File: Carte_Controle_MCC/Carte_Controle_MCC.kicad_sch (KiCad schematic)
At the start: 31 parts, among them J1 USB_C_Receptacle_USB2.0_16P, J2 Conn_ST_STDC14, J3 Conn_01x02_XT60, J4 Conn_01x04_moteur, U1 USBLC6-2SC6, U2 STM32G431CBUx

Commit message: Update 2
Correction of the schematic,
creation of new footprints,
Association of the footprints and the symbols
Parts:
- added H1, H2, H3, H4: MountingHole_Pad, MountingHole:MountingHole_3.2mm_M3_DIN965_Pad, symbol Mechanical:MountingHole_Pad
- C1, C10, C11, C2, C3, C4, C5, C6, C7, C8, C9: footprint (none) -> Capacitor_SMD:C_0201_0603Metric_Pad0.64x0.40mm_HandSolder
- C_IN1: renamed from C_IN; footprint (none) -> Capacitor_SMD:C_0201_0603Metric_Pad0.64x0.40mm_HandSolder
- C_OUT1: renamed from C_OUT; footprint (none) -> Capacitor_SMD:C_0201_0603Metric_Pad0.64x0.40mm_HandSolder
- C_VCC1: renamed from C_VCC; footprint (none) -> Capacitor_SMD:C_0201_0603Metric_Pad0.64x0.40mm_HandSolder
- D1, D2: footprint (none) -> Diode_SMD:D_0603_1608Metric_Pad1.05x0.95mm_HandSolder
- J1: footprint (none) -> Connector_USB:USB_C_Receptacle_G-Switch_GT-USB-7010ASV
- J2: footprint (none) -> Connector_PinHeader_1.27mm:PinHeader_2x07_P1.27mm_Vertical_SMD
- J3: footprint (none) -> Connector_AMASS:AMASS_XT60-M_1x02_P7.20mm_Vertical
- J4: footprint (none) -> Connector_JST:JST_EH_B4B-EH-A_1x04_P2.50mm_Vertical
- L1: footprint (none) -> Inductor_SMD:L_0805_2012Metric_Pad1.05x1.20mm_HandSolder
- R1, R2: value R_Small -> 5.1k; footprint (none) -> Resistor_SMD:R_0603_1608Metric_Pad0.98x0.95mm_HandSolder
- R_FBB1: renamed from R_FBB; footprint (none) -> Resistor_SMD:R_0603_1608Metric_Pad0.98x0.95mm_HandSolder
- R_FBT1: renamed from R_FBT; footprint (none) -> Resistor_SMD:R_0603_1608Metric_Pad0.98x0.95mm_HandSolder
- R_SW1: renamed from R_SW; footprint (none) -> Resistor_SMD:R_0603_1608Metric_Pad0.98x0.95mm_HandSolder
- U3: footprint (none) -> maker:wurth_171013801
- U4: footprint (none) -> maker:Gate_Driver_MIC4606-2YTS-TR
- U5: footprint (none) -> maker:Mosfet_FDMQ86530L
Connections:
- net USART_TX is gone; now on net USART_Tx: U2.31 (PA9)
- net +15V: now also U5.13 (D1/D4)
- net GND: now also U2.49 (VSS), H1.1, H2.1, H3.1, H4.1
- net S1/D2_INPUT: now also U5.14 (S1/D2)
- net S4/D3_INPUT: now also U5.15 (D3/S4)
- net USB_DM: now also U2.33 (PA11)
- net USB_DP: now also U2.34 (PA12)
- no-connect marks 40 -> 39
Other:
- note added: "Trous de Fixation"
- moved on the sheet: C10, C9, L1, R_SW1, U1

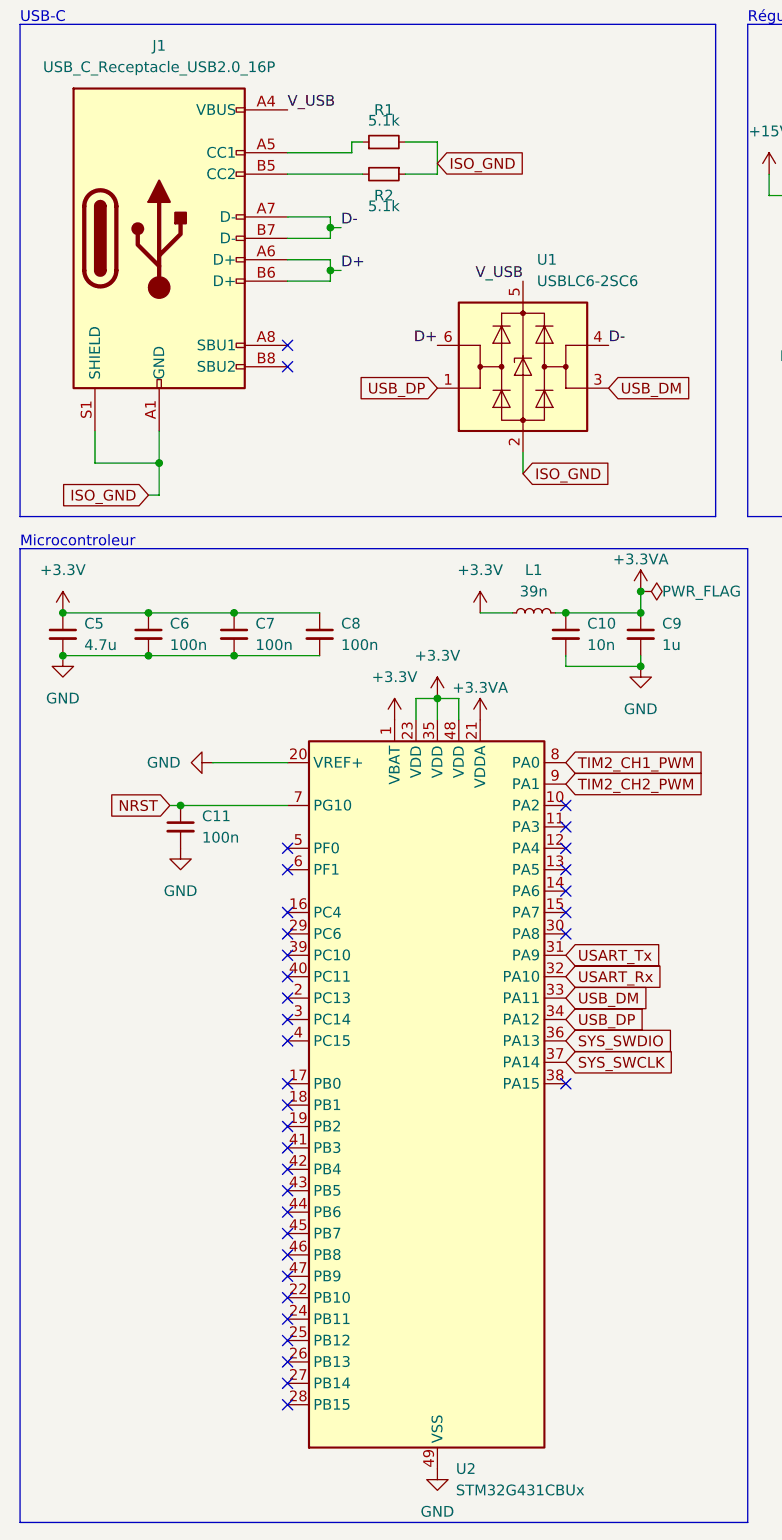
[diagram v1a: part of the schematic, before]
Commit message: routing of the PCB
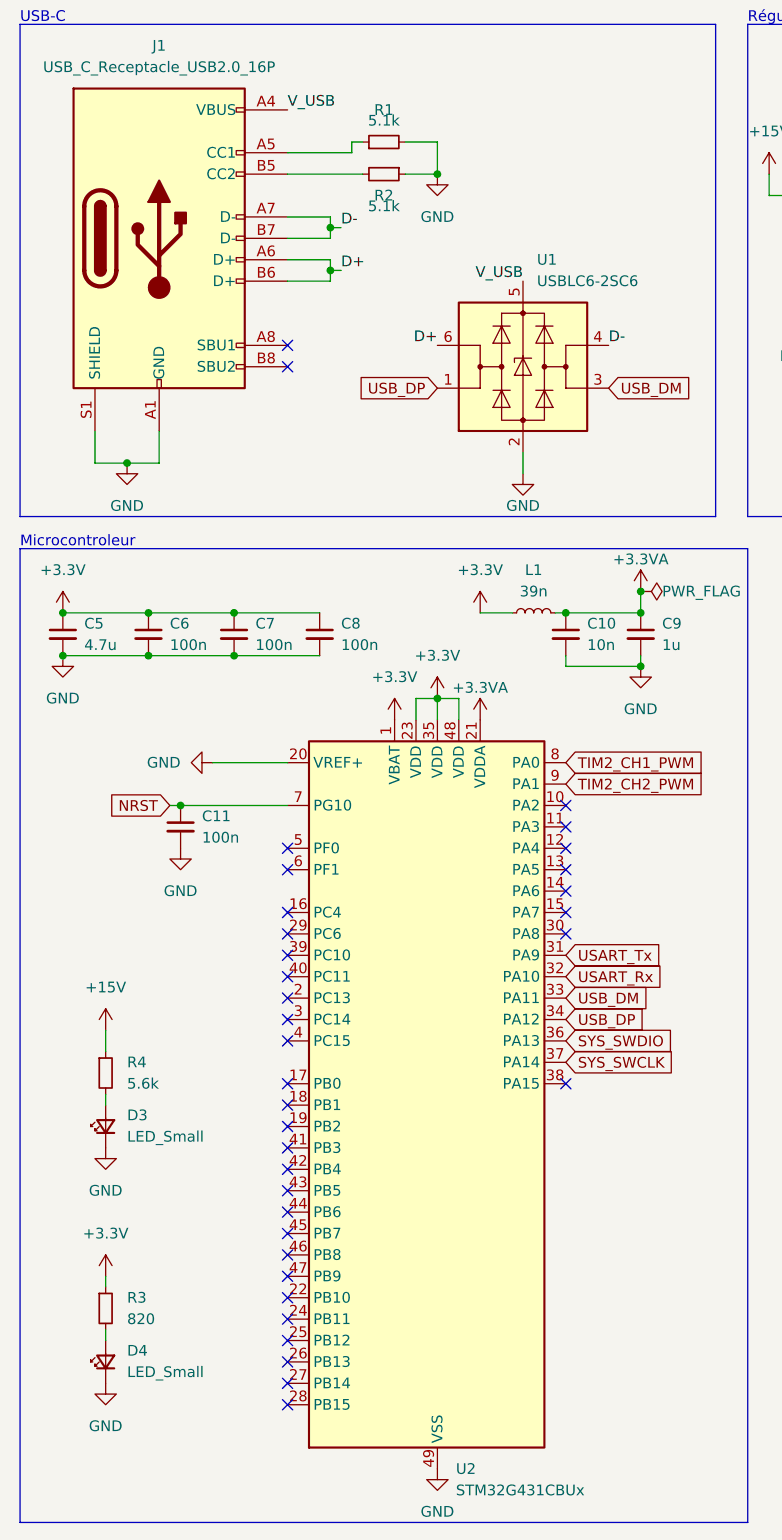
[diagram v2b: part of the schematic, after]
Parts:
- added D3, D4: LED_Small, LED_SMD:LED_0603_1608Metric_Pad1.05x0.95mm_HandSolder, symbol Device:LED_Small
- added R3: 820, Resistor_SMD:R_0603_1608Metric_Pad0.98x0.95mm_HandSolder, symbol Device:R_Small
- added R4: 5.6k, Resistor_SMD:R_0603_1608Metric_Pad0.98x0.95mm_HandSolder, symbol Device:R_Small
- J1: MPM (none) -> x
- U2: MPM (none) -> STM32G431CBU6
- U3: MPM (none) -> 171013801
- U4: MPM (none) -> MIC4606-2YTS-TR
- U5: MPM (none) -> FDMQ86530L
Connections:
- net ISO_GND is gone; now on net GND: J1.A1 (GND), J1.A12 (GND), J1.B1 (GND), J1.B12 (GND), J1.S1 (SHIELD), R1.2, R2.1, U1.2 (GND)
- net +15V: now also R4.1
- net +3.3V: now also R3.1
- net GND: now also D3.1 (K), D4.1 (K)
- new net: D3.2 (A), R4.2
- new net: D4.2 (A), R3.2
